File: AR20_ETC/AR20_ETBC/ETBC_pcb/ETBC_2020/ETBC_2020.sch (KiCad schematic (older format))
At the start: 31 parts, among them IC1 MC33931EK, J1 Conn_02x09_Top_Bottom, P1 MX23A12NF1, U1 ACM_2020

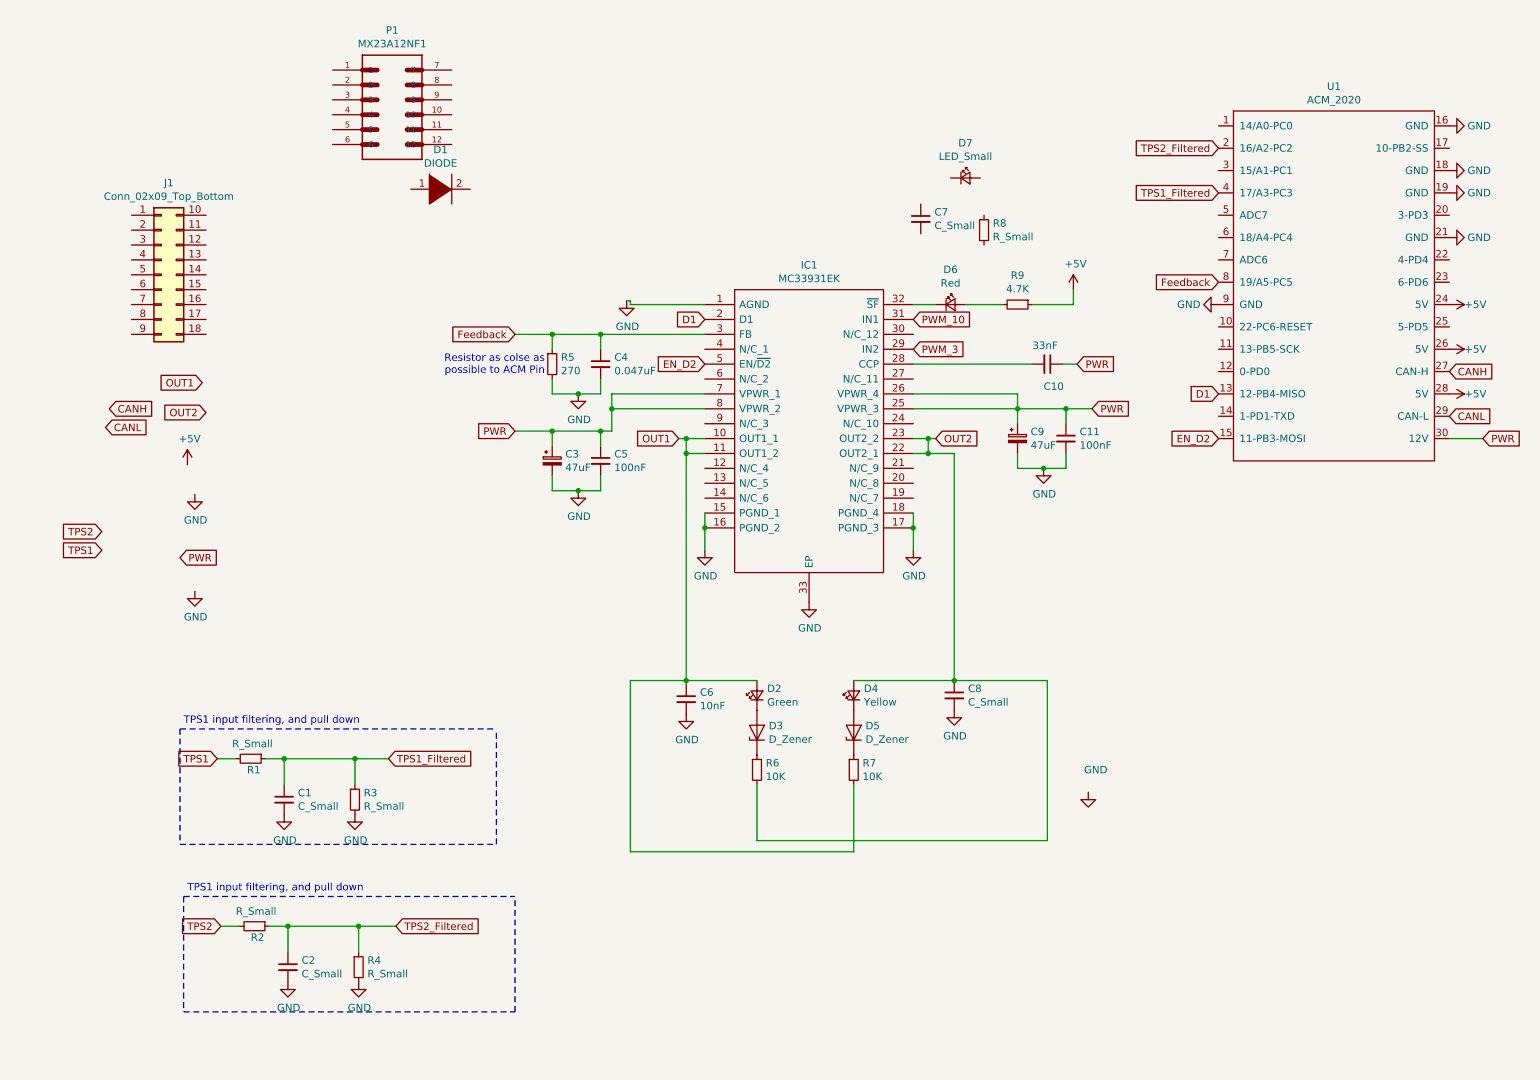
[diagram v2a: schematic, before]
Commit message: Se Changelog in description
Changed connector
Added Capacitors
Set footprints
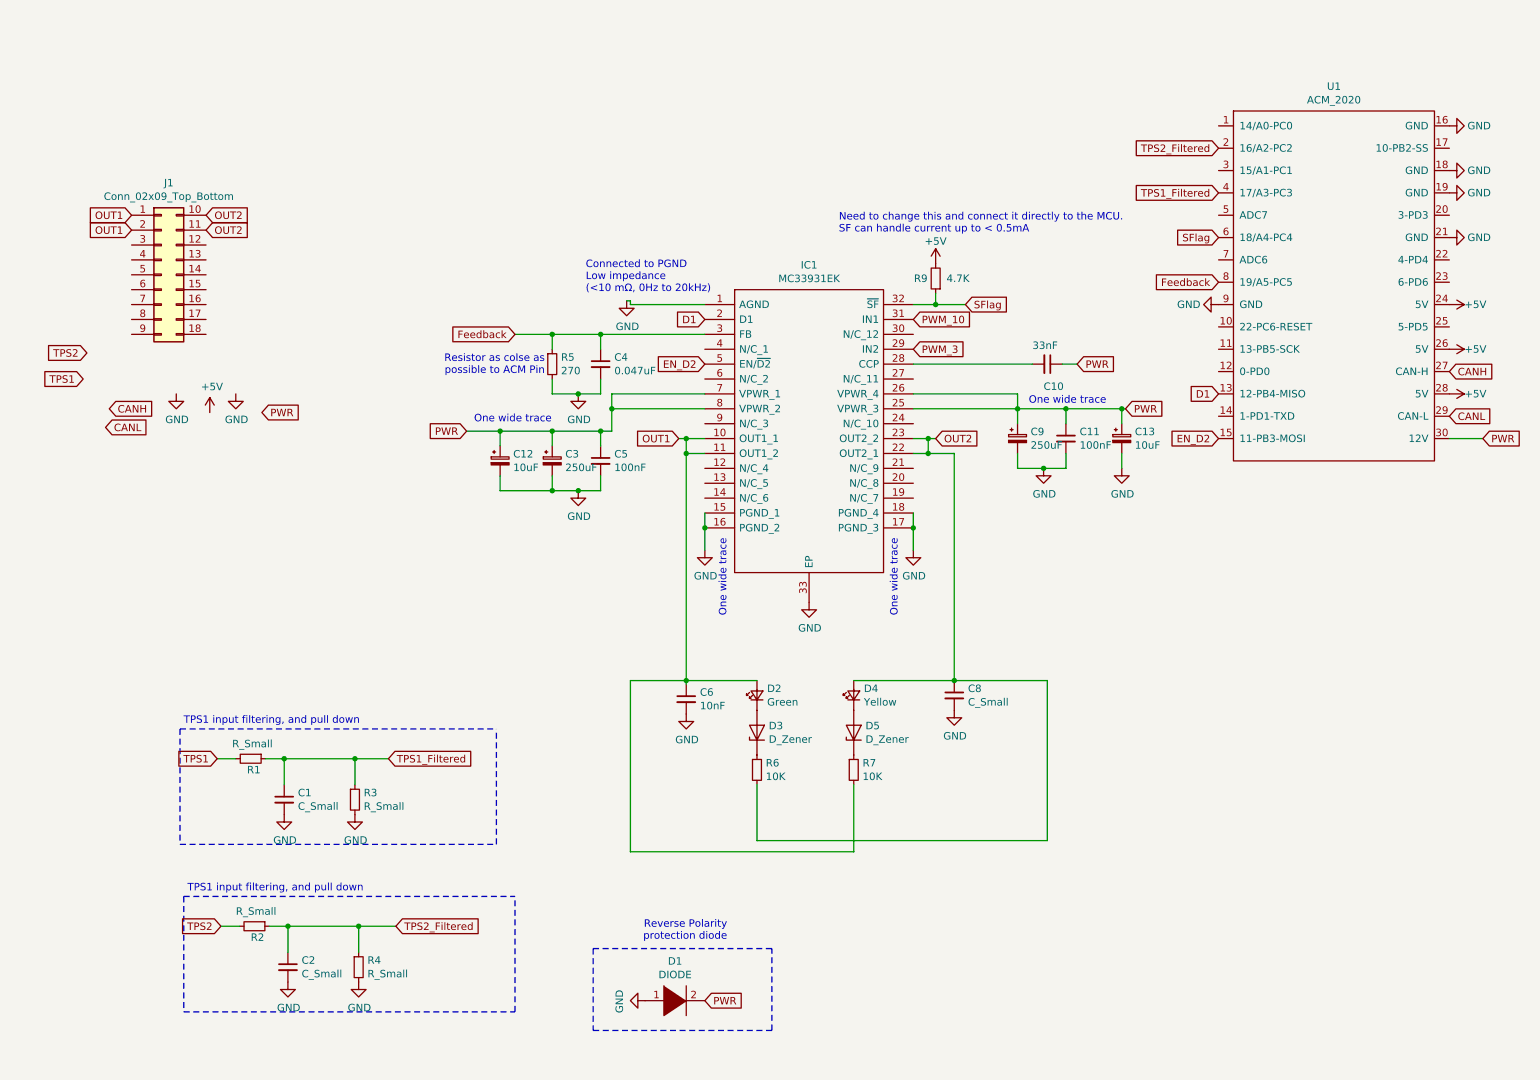
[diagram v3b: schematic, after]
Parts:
- removed C7: C_Small, Capacitor_SMD:C_0603_1608Metric_Pad1.05x0.95mm_HandSolder, symbol Device:C_Small
- removed D6: Red, symbol Device:LED_Small
- removed D7: LED_Small, symbol Device:LED_Small
- removed P1: MX23A12NF1, JAE_MX23A12NF1, symbol MX23A12NF1:MX23A12NF1
- removed R8: R_Small, Resistor_SMD:R_0603_1608Metric_Pad1.05x0.95mm_HandSolder, symbol Device:R_Small
- added C12, C13: 10uF, Capacitor_SMD:C_1206_3216Metric_Pad1.42x1.75mm_HandSolder, symbol Device:CP_Small
- C3, C9: value 47uF -> 250uF
- J1: footprint (none) -> ETBC_2020:JAE_MX23A18NF1
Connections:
- net +5V: now also R9.2; no longer R9.1
- net GND: now also D1.1 (K), C12.2, C13.2
- net OUT1: now also J1.1 (Pin_1), J1.2 (Pin_2)
- net OUT2: now also J1.10 (Pin_10), J1.11 (Pin_11)
- net PWR: now also D1.2 (A), C12.1, C13.1
- net SFlag: now reaches U1.6 (18/A4-PC4)
- net SFlag: now also IC1.32 (~SF), R9.1
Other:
- note added: "Connected to PGND\nLow impedance\n(<10 mΩ, 0Hz to 20kHz)"
- note added: "Need to change this and connect it directly to the MCU.\nSF can handle current up to < 0.5mA"
- note added: "One wide trace"
- note added: "Reverse Polarity\nprotection diode"
- moved on the sheet: D1, R9
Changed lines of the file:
@@
-$EndComp
-$Comp
-L MX23A12NF1:MX23A12NF1 P1
-U 1 1 5E29DC77
-P 2975 1150
-F 0 "P1" H 2975 1667 50  0000 C CNN
-F 1 "MX23A12NF1" H 2975 1576 50  0000 C CNN
-F 2 "JAE_MX23A12NF1" H 2975 1150 50  0001 L BNN
-F 3 "" H 2975 1150 50  0001 L BNN
-	1    2975 1150
-	1    0    0    -1
 $EndComp
 $Comp
@@
 L pspice:DIODE D1
 U 1 1 5E2F58CD
-P 3300 1700
-F 0 "D1" H 3300 1965 50  0000 C CNN
-F 1 "DIODE" H 3300 1874 50  0000 C CNN
-F 2 "" H 3300 1700 50  0001 C CNN
-F 3 "~" H 3300 1700 50  0001 C CNN
-	1    3300 1700
+P 4875 7150
+F 0 "D1" H 4875 7415 50  0000 C CNN
+F 1 "DIODE" H 4875 7324 50  0000 C CNN
+F 2 "" H 4875 7150 50  0001 C CNN
+F 3 "~" H 4875 7150 50  0001 C CNN
+	1    4875 7150
 	1    0    0    -1
 $EndComp
@@
 	4575 2450 4575 2475
 $Comp
-L Device:LED_Small D7
-U 1 1 5E2F949D
-P 6825 1625
-F 0 "D7" H 6825 1860 50  0000 C CNN
-F 1 "LED_Small" H 6825 1769 50  0000 C CNN
-F 2 "" V 6825 1625 50  0001 C CNN
-F 3 "~" V 6825 1625 50  0001 C CNN
-	1    6825 1625
-	1    0    0    -1
-$EndComp
-$Comp
-L Device:R_Small R8
-U 1 1 5E2FA160
-P 6950 1975
-F 0 "R8" H 7009 2021 50  0000 L CNN
-F 1 "R_Small" H 7009 1930 50  0000 L CNN
-F 2 "Resistor_SMD:R_0603_1608Metric_Pad1.05x0.95mm_HandSolder" H 6950 1975 50  0001 C CNN
-F 3 "~" H 6950 1975 50  0001 C CNN
-	1    6950 1975
-	1    0    0    -1
-$EndComp
-$Comp
-L Device:C_Small C7
-U 1 1 5E2FA2C1
-P 6525 1900
-F 0 "C7" H 6617 1946 50  0000 L CNN
-F 1 "C_Small" H 6617 1855 50  0000 L CNN
-F 2 "Capacitor_SMD:C_0603_1608Metric_Pad1.05x0.95mm_HandSolder" H 6525 1900 50  0001 C CNN
-F 3 "~" H 6525 1900 50  0001 C CNN
-	1    6525 1900
-	1    0    0    -1
-$EndComp
-$Comp
 L Device:C_Small C4
 U 1 1 5E2FA7AE
@@
 	4375 3725 4375 3625
 Connection ~ 4225 3725
-Wire Wire Line
-	3800 3325 4050 3325
 Wire Wire Line
 	4050 3425 4050 3325
@@
 $EndComp
 $Comp
-L power:GND #PWR0108
-U 1 1 5E325CFF
-P 7650 5750
-F 0 "#PWR0108" H 7650 5500 50  0001 C CNN
-F 1 "GND" H 7700 5900 50  0000 C CNN
-F 2 "" H 7650 5750 50  0001 C CNN
-F 3 "" H 7650 5750 50  0001 C CNN
-	1    7650 5750
-	1    0    0    -1
-$EndComp
-$Comp
 L power:GND #PWR0109
 U 1 1 5E32970E
@@
 P 4050 3525
 F 0 "C3" H 4138 3571 50  0000 L CNN
-F 1 "47uF" H 4138 3480 50  0000 L CNN
+F 1 "250uF" H 4138 3480 50  0000 L CNN
 F 2 "Capacitor_SMD:C_0603_1608Metric_Pad1.05x0.95mm_HandSolder" H 4050 3525 50  0001 C CNN
 F 3 "~" H 4050 3525 50  0001 C CNN
@@
 	1    0    0    -1
 $EndComp
-$Comp
-L power:GND #PWR0110
-U 1 1 5E334426
-P 7350 3575
-F 0 "#PWR0110" H 7350 3325 50  0001 C CNN
-F 1 "GND" H 7355 3402 50  0000 C CNN
-F 2 "" H 7350 3575 50  0001 C CNN
-F 3 "" H 7350 3575 50  0001 C CNN
-	1    7350 3575
-	1    0    0    -1
-$EndComp
 Wire Wire Line
 	7175 3475 7175 3575
@@
 P 7175 3375
 F 0 "C9" H 7263 3421 50  0000 L CNN
-F 1 "47uF" H 7263 3330 50  0000 L CNN
+F 1 "250uF" H 7263 3330 50  0000 L CNN
 F 2 "Capacitor_SMD:C_0603_1608Metric_Pad1.05x0.95mm_HandSolder" H 7175 3375 50  0001 C CNN
 F 3 "~" H 7175 3375 50  0001 C CNN
@@
 Wire Wire Line
 	7175 3175 7500 3175
-$Comp
-L Device:LED_Small D6
-U 1 1 5E33755A
-P 6725 2475
-F 0 "D6" H 6725 2710 50  0000 C CNN
-F 1 "Red" H 6725 2619 50  0000 C CNN
-F 2 "" V 6725 2475 50  0001 C CNN
-F 3 "~" V 6725 2475 50  0001 C CNN
-	1    6725 2475
-	1    0    0    -1
-$EndComp
 Wire Wire Line
 	6475 2475 6625 2475
@@
 L Device:R_Small R9
 U 1 1 5E339186
-P 7175 2475
-F 0 "R9" V 6979 2475 50  0000 C CNN
-F 1 "4.7K" V 7070 2475 50  0000 C CNN
-F 2 "Resistor_SMD:R_0603_1608Metric_Pad1.05x0.95mm_HandSolder" H 7175 2475 50  0001 C CNN
-F 3 "~" H 7175 2475 50  0001 C CNN
-	1    7175 2475
-	0    1    1    0
-$EndComp
-Wire Wire Line
-	6825 2475 7075 2475
+P 6625 2300
+F 0 "R9" H 6725 2300 50  0000 C CNN
+F 1 "4.7K" H 6475 2300 50  0000 C CNN
+F 2 "Resistor_SMD:R_0603_1608Metric_Pad1.05x0.95mm_HandSolder" H 6625 2300 50  0001 C CNN
+F 3 "~" H 6625 2300 50  0001 C CNN
+	1    6625 2300
+	-1   0    0    1
+$EndComp
 $Comp
 L power:+5V #PWR0111
 U 1 1 5E33B1A4
-P 7550 2375
-F 0 "#PWR0111" H 7550 2225 50  0001 C CNN
-F 1 "+5V" H 7565 2548 50  0000 C CNN
-F 2 "" H 7550 2375 50  0001 C CNN
-F 3 "" H 7550 2375 50  0001 C CNN
-	1    7550 2375
-	1    0    0    -1
-$EndComp
-Wire Wire Line
-	7275 2475 7550 2475
-Wire Wire Line
-	7550 2475 7550 2375
+P 6625 2200
+F 0 "#PWR0111" H 6625 2050 50  0001 C CNN
+F 1 "+5V" H 6625 2350 50  0000 C CNN
+F 2 "" H 6625 2200 50  0001 C CNN
+F 3 "" H 6625 2200 50  0001 C CNN
+	1    6625 2200
+	1    0    0    -1
+$EndComp
 $Comp
 L Device:R_Small R6
@@
 Text GLabel 5075 2875 0    50   Input ~ 0
 EN_D2
-Text GLabel 3800 3325 0    50   Input ~ 0
+Text GLabel 3475 3325 0    50   Input ~ 0
 PWR
-Text GLabel 7675 3175 2    50   Input ~ 0
+Text GLabel 7900 3175 2    50   Input ~ 0
 PWR
-Wire Wire Line
-	7500 3175 7675 3175
 Connection ~ 7500 3175
 $Comp
@@
 	3000 6650 2750 6650
 Connection ~ 2750 6650
-Text GLabel 1700 3000 0    50   Input ~ 0
+Text GLabel 1225 1875 0    50   Input ~ 0
 OUT1
-Text GLabel 1725 3200 0    50   Input ~ 0
+Text GLabel 1725 1875 2    50   Input ~ 0
 OUT2
 $Comp
 L power:+5V #PWR0124
 U 1 1 5E3A949C
-P 1600 3550
-F 0 "#PWR0124" H 1600 3400 50  0001 C CNN
-F 1 "+5V" H 1615 3723 50  0000 C CNN
-F 2 "" H 1600 3550 50  0001 C CNN
-F 3 "" H 1600 3550 50  0001 C CNN
-	1    1600 3550
+P 1750 3200
+F 0 "#PWR0124" H 1750 3050 50  0001 C CNN
+F 1 "+5V" H 1765 3373 50  0000 C CNN
+F 2 "" H 1750 3200 50  0001 C CNN
+F 3 "" H 1750 3200 50  0001 C CNN
+	1    1750 3200
 	1    0    0    -1
 $EndComp
@@
 L power:GND #PWR0125
 U 1 1 5E3A9F0C
-P 1650 3750
-F 0 "#PWR0125" H 1650 3500 50  0001 C CNN
-F 1 "GND" H 1655 3577 50  0000 C CNN
-F 2 "" H 1650 3750 50  0001 C CNN
-F 3 "" H 1650 3750 50  0001 C CNN
-	1    1650 3750
-	1    0    0    -1
-$EndComp
-Text GLabel 1025 4125 0    50   Input ~ 0
+P 1925 3075
+F 0 "#PWR0125" H 1925 2825 50  0001 C CNN
+F 1 "GND" H 1930 2902 50  0000 C CNN
+F 2 "" H 1925 3075 50  0001 C CNN
+F 3 "" H 1925 3075 50  0001 C CNN
+	1    1925 3075
+	1    0    0    -1
+$EndComp
+Text GLabel 900  2975 0    50   Input ~ 0
 TPS1
-Text GLabel 1025 4000 0    50   Input ~ 0
+Text GLabel 925  2800 0    50   Input ~ 0
 TPS2
-Text GLabel 1550 4175 2    50   Input ~ 0
+Text GLabel 2100 3200 2    50   Input ~ 0
 PWR
 $Comp
 L power:GND #PWR0126
 U 1 1 5E3AA8D4
-P 1650 4400
-F 0 "#PWR0126" H 1650 4150 50  0001 C CNN
-F 1 "GND" H 1655 4227 50  0000 C CNN
-F 2 "" H 1650 4400 50  0001 C CNN
-F 3 "" H 1650 4400 50  0001 C CNN
-	1    1650 4400
+P 1525 3075
+F 0 "#PWR0126" H 1525 2825 50  0001 C CNN
+F 1 "GND" H 1530 2902 50  0000 C CNN
+F 2 "" H 1525 3075 50  0001 C CNN
+F 3 "" H 1525 3075 50  0001 C CNN
+	1    1525 3075
 	1    0    0    -1
 $EndComp
@@
 F 0 "J1" H 1475 2892 50  0000 C CNN
 F 1 "Conn_02x09_Top_Bottom" H 1475 2801 50  0000 C CNN
-F 2 "" H 1425 2275 50  0001 C CNN
+F 2 "ETBC_2020:JAE_MX23A18NF1" H 1425 2275 50  0001 C CNN
 F 3 "~" H 1425 2275 50  0001 C CNN
 	1    1425 2275
@@
 Text Notes 4000 2950 2    50   ~ 0
 Resistor as colse as\npossible to ACM Pin
+Text Notes 5225 6750 2    50   ~ 0
+Reverse Polarity\nprotection diode
+Text GLabel 5075 7150 2    50   Input ~ 0
+PWR
+$Comp
+L power:GND #PWR0127
+U 1 1 5E382CFF
+P 4675 7150
+F 0 "#PWR0127" H 4675 6900 50  0001 C CNN
+F 1 "GND" H 4680 6977 50  0000 C CNN
+F 2 "" H 4675 7150 50  0001 C CNN
+F 3 "" H 4675 7150 50  0001 C CNN
+	1    4675 7150
+	0    1    1    0
+$EndComp
+$Comp
+L Device:CP_Small C12
+U 1 1 5E386C55
+P 3700 3525
+F 0 "C12" H 3788 3571 50  0000 L CNN
+F 1 "10uF" H 3788 3480 50  0000 L CNN
+F 2 "Capacitor_SMD:C_1206_3216Metric_Pad1.42x1.75mm_HandSolder" H 3700 3525 50  0001 C CNN
+F 3 "~" H 3700 3525 50  0001 C CNN
+	1    3700 3525
+	1    0    0    -1
+$EndComp
+Wire Wire Line
+	3475 3325 3700 3325
+Wire Wire Line
+	7500 3175 7875 3175
+$Comp
+L Device:CP_Small C13
+U 1 1 5E38C578
+P 7875 3375
+F 0 "C13" H 7963 3421 50  0000 L CNN
+F 1 "10uF" H 7963 3330 50  0000 L CNN
+F 2 "Capacitor_SMD:C_1206_3216Metric_Pad1.42x1.75mm_HandSolder" H 7875 3375 50  0001 C CNN
+F 3 "~" H 7875 3375 50  0001 C CNN
+	1    7875 3375
+	1    0    0    -1
+$EndComp
+Wire Wire Line
+	7875 3275 7875 3175
+Connection ~ 7875 3175
+Wire Wire Line
+	7875 3175 7900 3175
+Wire Wire Line
+	7875 3475 7875 3575
+$Comp
+L power:GND #PWR0110
+U 1 1 5E334426
+P 7350 3575
+F 0 "#PWR0110" H 7350 3325 50  0001 C CNN
+F 1 "GND" H 7355 3402 50  0000 C CNN
+F 2 "" H 7350 3575 50  0001 C CNN
+F 3 "" H 7350 3575 50  0001 C CNN
+	1    7350 3575
+	1    0    0    -1
+$EndComp
+$Comp
+L power:GND #PWR0128
+U 1 1 5E39393D
+P 7875 3575
+F 0 "#PWR0128" H 7875 3325 50  0001 C CNN
+F 1 "GND" H 7880 3402 50  0000 C CNN
+F 2 "" H 7875 3575 50  0001 C CNN
+F 3 "" H 7875 3575 50  0001 C CNN
+	1    7875 3575
+	1    0    0    -1
+$EndComp
+Wire Wire Line
+	3700 3625 3700 3725
+Wire Wire Line
+	3700 3725 4050 3725
+Connection ~ 4050 3725
+Wire Wire Line
+	3700 3425 3700 3325
+Connection ~ 3700 3325
+Wire Wire Line
+	3700 3325 4050 3325
+Wire Notes Line
+	4325 6800 4325 7350
+Wire Notes Line
+	4325 7350 5525 7350
+Wire Notes Line
+	5525 7350 5525 6800
+Wire Notes Line
+	5525 6800 4325 6800
+Text GLabel 1225 1975 0    50   Input ~ 0
+OUT1
+Text GLabel 1725 1975 2    50   Input ~ 0
+OUT2
+Text Notes 4275 2400 0    50   ~ 0
+Connected to PGND\nLow impedance\n(<10 mΩ, 0Hz to 20kHz)
+Text Notes 3525 3275 0    50   ~ 0
+One wide trace
+Text Notes 7250 3150 0    50   ~ 0
+One wide trace
+Text Notes 5225 4050 3    50   ~ 0
+One wide trace
+Text Notes 6375 4050 3    50   ~ 0
+One wide trace
+Text Notes 5975 2000 0    50   ~ 0
+Need to change this and connect it directly to the MCU.\nSF can handle current up to < 0.5mA
+Wire Wire Line
+	6625 2400 6625 2475
+Wire Wire Line
+	6625 2475 6825 2475
+Connection ~ 6625 2475
+Text GLabel 6825 2475 2    50   Input ~ 0
+SFlag
+Text GLabel 8525 2025 0    50   Input ~ 0
+SFlag
 $EndSCHEMATC

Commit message: Value change
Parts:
- C8: value C_Small -> 10nF
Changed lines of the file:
@@
 P 6750 5100
 F 0 "C8" H 6842 5146 50  0000 L CNN
-F 1 "C_Small" H 6842 5055 50  0000 L CNN
+F 1 "10nF" H 6842 5055 50  0000 L CNN
 F 2 "Capacitor_SMD:C_0603_1608Metric_Pad1.05x0.95mm_HandSolder" H 6750 5100 50  0001 C CNN
 F 3 "~" H 6750 5100 50  0001 C CNN

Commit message: Changed footprint
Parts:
- U1: footprint (none) -> ETBC_2020:ACM_2020_Footprint_wo_silk
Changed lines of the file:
@@
 F 0 "U1" H 9300 6140 50  0000 C CNN
 F 1 "ACM_2020" H 9300 6049 50  0000 C CNN
-F 2 "" H 9275 3575 50  0001 C CNN
+F 2 "ETBC_2020:ACM_2020_Footprint_wo_silk" H 9275 3575 50  0001 C CNN
 F 3 "" H 9275 3575 50  0001 C CNN
 	1    9275 3575
